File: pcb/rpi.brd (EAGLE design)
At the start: 88 x 85 mm, 27 parts, among them IC1 LD117AS33TR, SW1 324_SW, SW20 324_SW, U5 CH340C

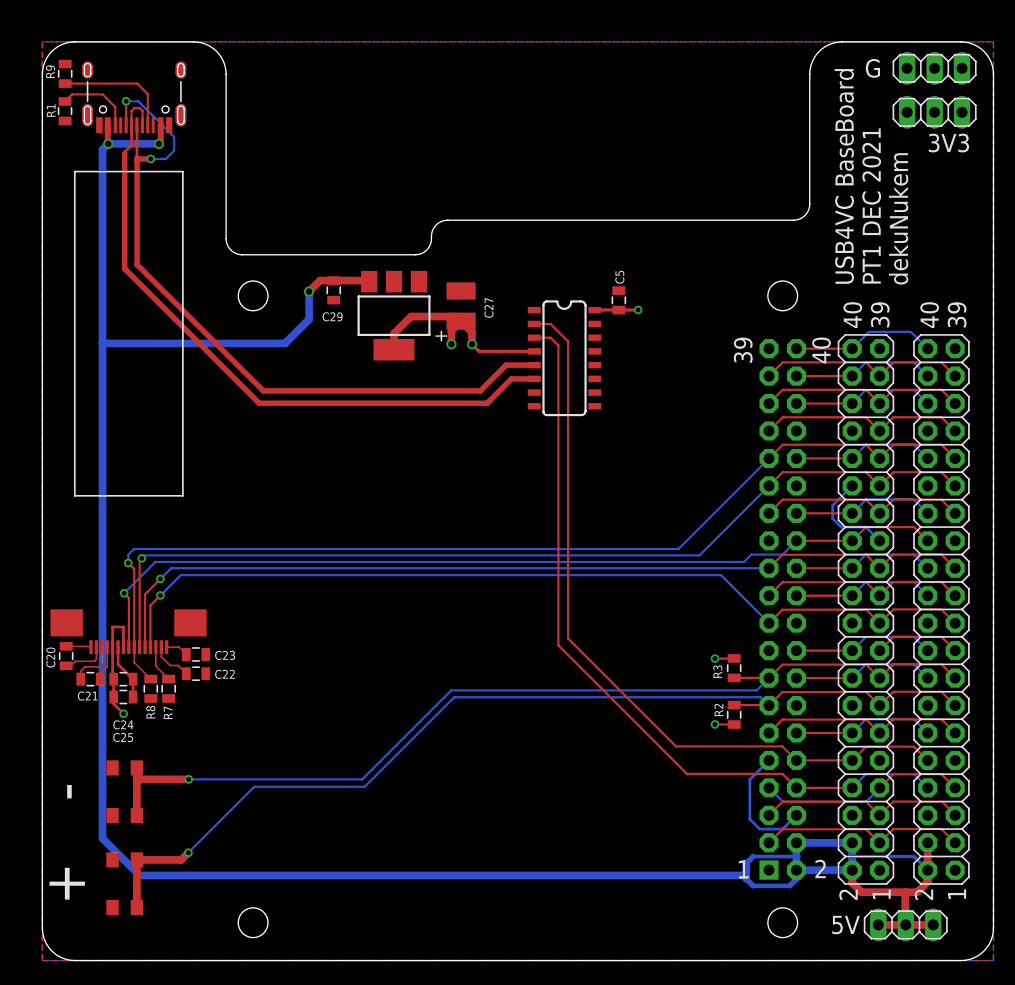
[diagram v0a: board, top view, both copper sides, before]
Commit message: updated baseboard, added power buttons
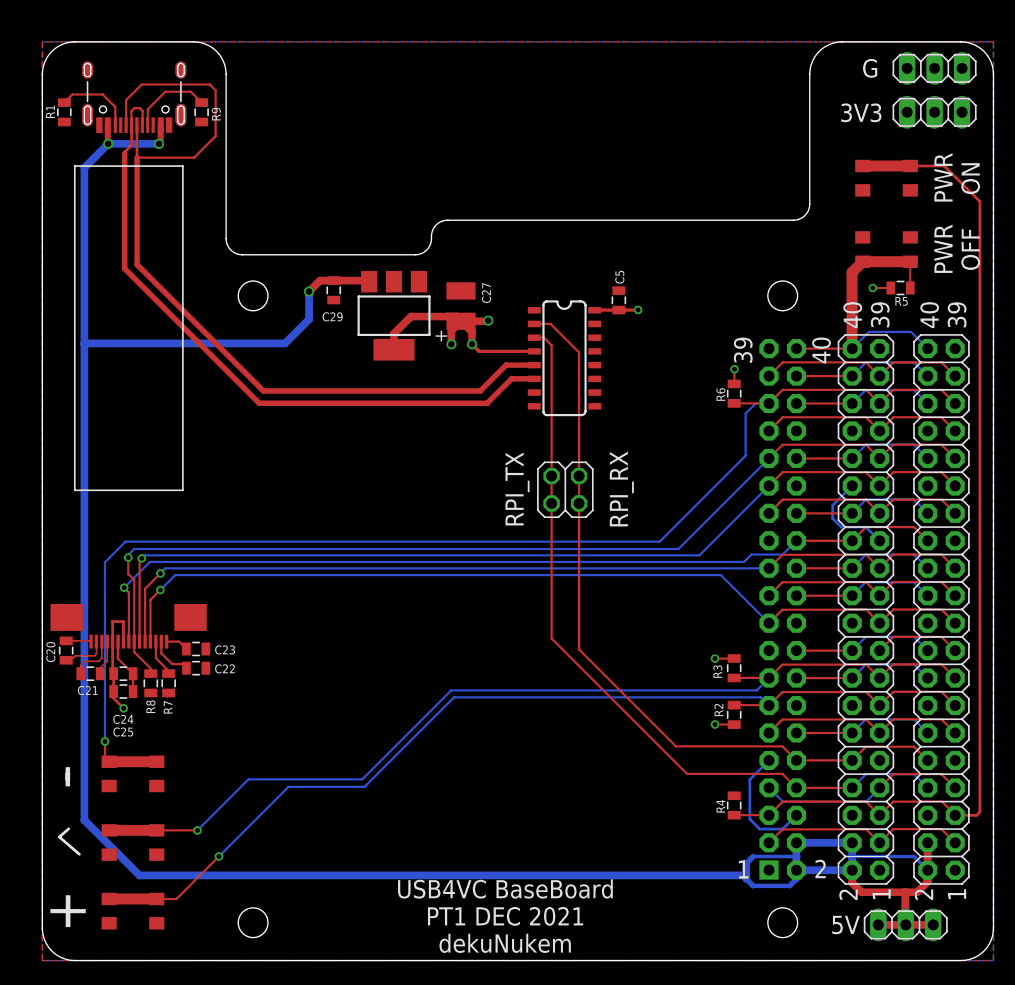
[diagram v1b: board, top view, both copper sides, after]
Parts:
- added JP7: (no value), pinhead:2X02
- added R4, R5, R6: 390K, SparkFun-Passives:0805
- added SW2, SW3, SW4: 324_SW, 3pos_slide_switch_centered:342_SWICH_FOOT
- moved R9 13.1 mm to (14.7, 78.5), turned to 270 degrees
- moved SW20 4.76 mm to (8.38, 10.9), turned to 0 degrees
- moved SW1 2.65 mm to (8.38, 4.57), turned to 0 degrees
- moved C20 0.51 mm to (2.20, 28.7)
- moved C21 0.51 mm to (4.45, 26.5)
- moved C22 0.51 mm to (14.2, 27.1)
- moved C23 0.51 mm to (14.2, 28.8)
- moved C24 0.51 mm to (7.49, 26.5)
- moved C25 0.51 mm to (7.49, 24.9)
- moved R7 0.51 mm to (11.7, 25.7)
- moved R8 0.51 mm to (10.0, 25.7)
- moved U2 0.51 mm to (8.00, 29.5)
- moved R1 0.13 mm to (2.03, 78.5)
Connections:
- net N$11 renamed ENTER_BUTTON
- net N$34 renamed PLUS_BUTTON
- removed net N$20: JP1.35, JP2.35, PCB1.P$35
- removed net UART0_RX: JP1.10, JP2.10, PCB1.P$10, U5.2
- removed net UART0_TX: JP1.8, JP2.8, PCB1.P$8, U5.3
- new net MINUS_BUTTON: JP1.35, JP2.35, PCB1.P$35, R6.1, SW4.P$2, SW4.P$3
- new net RPI_RX: JP1.10, JP2.10, JP7.1, JP7.2, PCB1.P$10, U5.2
- new net RPI_TX: JP1.8, JP2.8, JP7.3, JP7.4, PCB1.P$8, U5.3
- net +3V3: now also R5.2, R6.2
- net GND: now also SW2.P$1, SW2.P$4, SW3.P$1, SW3.P$4, SW4.P$1, SW4.P$4
- net N$32: now also R5.1, SW3.P$2, SW3.P$3
- net N$6: now also R4.1, SW2.P$2, SW2.P$3
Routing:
- net MINUS_BUTTON: track 0.00 -> 115.4 mm, vias 0 -> 1
- net N$6: track 19.4 -> 93.7 mm
- net UART0_TX: track 71.0 -> 0.00 mm
- net RPI_TX: track 0.00 -> 70.6 mm
- net UART0_RX: track 70.3 -> 0.00 mm
- net RPI_RX: track 0.00 -> 70.3 mm
- net N$20: track 19.3 -> 0.00 mm
- net N$32: track 13.4 -> 28.7 mm
- net N$1: track 68.6 -> 79.2 mm, vias 2 -> 0
- net +3V3: track 46.5 -> 52.1 mm, vias 6 -> 9
- net N$2: track 10.9 -> 7.53 mm
- net +5V: track 218.2 -> 221.3 mm
- net N$16: track 88.4 -> 87.9 mm
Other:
- board text added: "PWR OFF"
- board text added: "PWR ON"
- board text added: "RPI_RX"
- board text added: "RPI_TX"

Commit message: added i2c pullups, cleanup
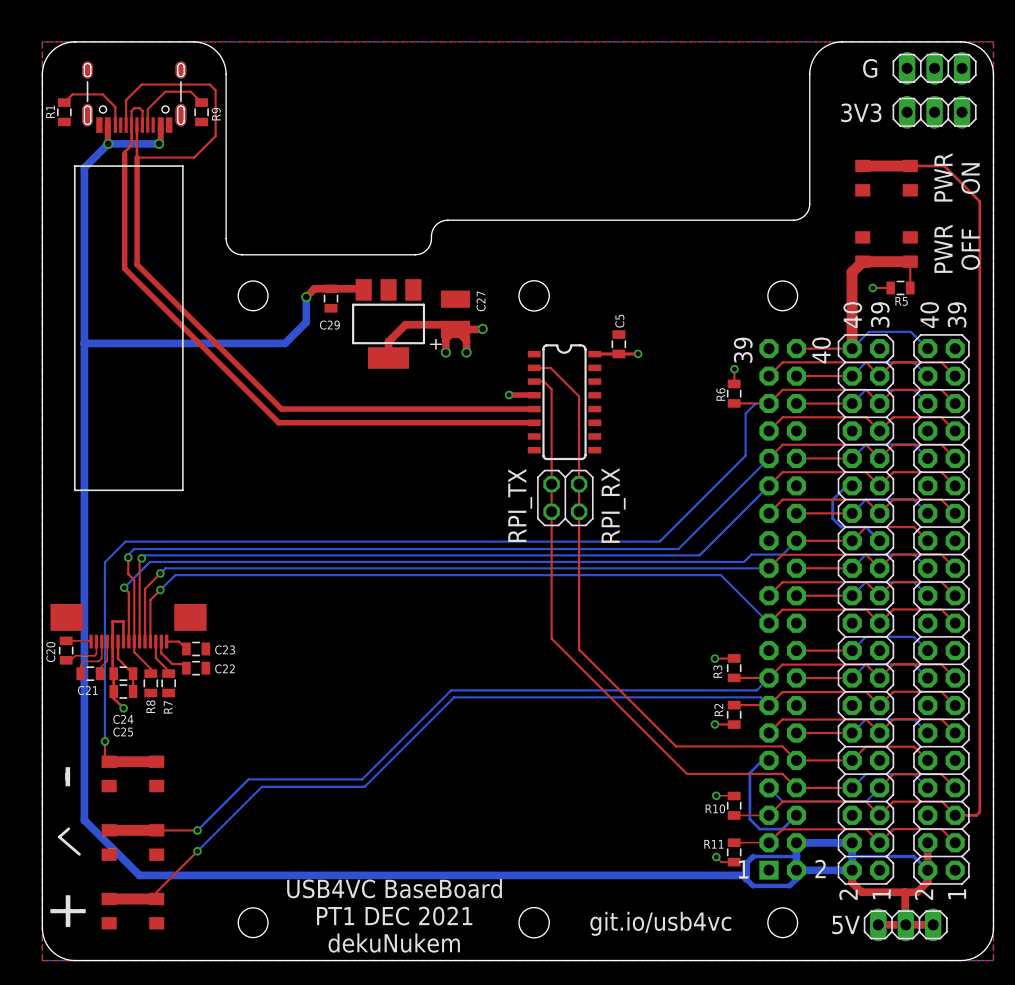
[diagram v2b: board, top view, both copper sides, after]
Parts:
- removed R4: 390K, SparkFun-Passives:0805
- added R10, R11: 5.1K, joyAnalog:0805
- added U$2, U$3: M2.5HOLE, f1c100s:M2.5HOLE
- moved C5 4.06 mm to (53.3, 57.0)
- moved U5 4.06 mm to (48.3, 51.7)
- moved C27 0.92 mm to (38.2, 59.8)
- moved IC1 0.92 mm to (32.0, 58.9)
- moved C29 0.80 mm to (26.7, 61.3)
- moved JP7 0.76 mm to (48.4, 42.8)
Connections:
- net +3V3: now also R10.1, R11.1
- net N$5: now also R11.2
- net N$6: now also R10.2; no longer R4.1
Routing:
- net +3V3: track 52.1 -> 43.9 mm, vias 9 -> 12
- net RPI_RX: track 70.3 -> 66.2 mm
- net RPI_TX: track 70.6 -> 66.5 mm
- net N$5: track 19.3 -> 22.5 mm
- net +5V: track 221.3 -> 220.3 mm
- net GND: track 25.6 -> 26.2 mm
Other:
- board text added: "git.io/usb4vc"

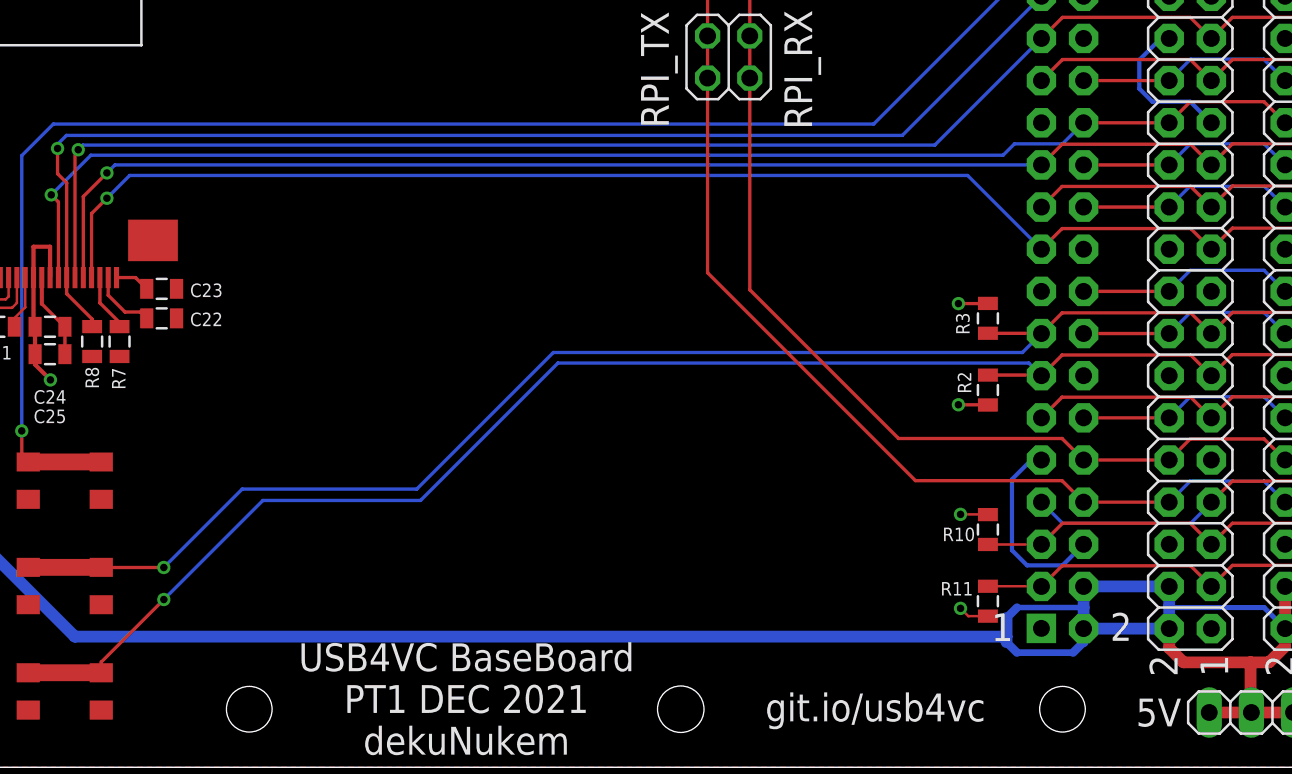
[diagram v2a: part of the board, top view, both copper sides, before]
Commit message: finished ADB protocol board
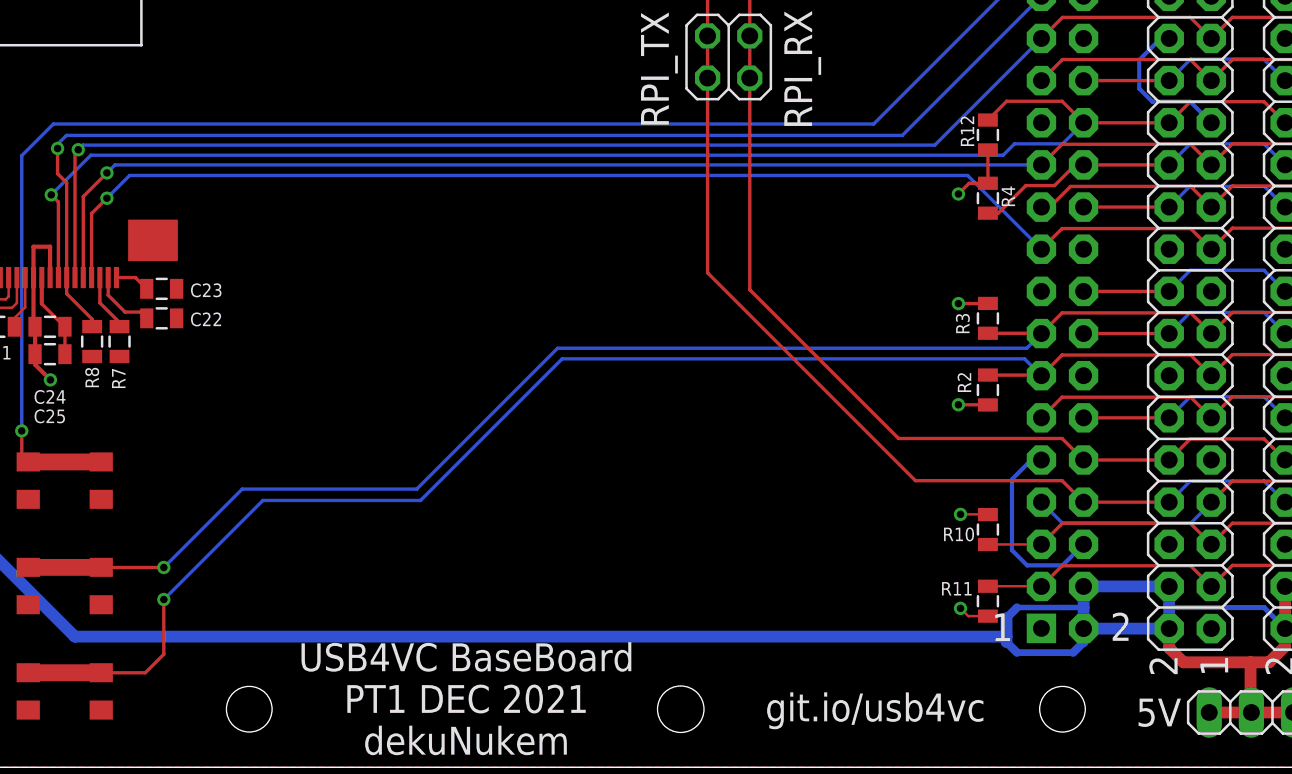
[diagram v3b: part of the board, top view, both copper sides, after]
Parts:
- added R12, R4: 5.1K, joyAnalog:0805
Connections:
- net +3V3: now also R12.1, R4.1
- net N$26: now also R4.2
- net N$27: now also R12.2
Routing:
- net N$26: track 13.2 -> 20.2 mm
- net N$27: track 82.4 -> 89.1 mm
- net +3V3: track 43.9 -> 47.9 mm, vias 12 -> 13
- net PLUS_BUTTON: track 92.0 -> 93.8 mm
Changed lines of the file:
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@@
 <element name="U$2" library="f1c100s" package="M2.5HOLE" value="M2.5HOLE" x="45.5" y="3.5" smashed="yes"/>
 <element name="U$3" library="f1c100s" package="M2.5HOLE" value="M2.5HOLE" x="45.5" y="61.5" smashed="yes"/>
+<element name="R4" library="joyAnalog" package="0805" value="5.1K" x="64.008" y="34.29" smashed="yes" rot="R270">
+<attribute name="NAME" x="64.8335" y="35.052" size="0.8128" layer="25" rot="R270"/>
+</element>
+<element name="R12" library="joyAnalog" package="0805" value="5.1K" x="64.008" y="38.1" smashed="yes" rot="R90">
+<attribute name="NAME" x="63.1825" y="37.338" size="0.8128" layer="25" rot="R90"/>
+</element>
 </elements>
 <signals>
@@
 <wire x1="43.18" y1="52.324" x2="45.4854" y2="52.324" width="0.508" layer="1"/>
 <wire x1="45.4854" y1="52.324" x2="45.5108" y2="52.2986" width="0.508" layer="1"/>
+<contactref element="R12" pad="1"/>
+<contactref element="R4" pad="1"/>
+<via x="62.23" y="34.544" extent="1-16" drill="0.45"/>
+<wire x1="64.008" y1="37.2" x2="64.008" y2="35.19" width="0.2032" layer="1"/>
+<wire x1="62.23" y1="34.544" x2="62.876" y2="35.19" width="0.2032" layer="1"/>
+<wire x1="62.876" y1="35.19" x2="64.008" y2="35.19" width="0.2032" layer="1"/>
 </signal>
 <signal name="+5V">
@@
 <wire x1="64.008" y1="26.151" x2="67.2174" y2="26.151" width="0.2032" layer="1"/>
 <wire x1="67.2174" y1="26.151" x2="67.2318" y2="26.1366" width="0.2032" layer="1"/>
-<wire x1="67.2318" y1="26.1366" x2="66.0888" y2="24.9936" width="0.2032" layer="16"/>
-<wire x1="66.0888" y1="24.9936" x2="37.8206" y2="24.9936" width="0.2032" layer="16"/>
+<wire x1="67.2318" y1="26.1366" x2="66.3428" y2="25.2476" width="0.2032" layer="16"/>
+<wire x1="66.3428" y1="25.2476" x2="38.0746" y2="25.2476" width="0.2032" layer="16"/>
 <via x="14.351" y="12.0396" extent="1-16" drill="0.45"/>
-<wire x1="37.8206" y1="24.9936" x2="29.591" y2="16.764" width="0.2032" layer="16"/>
+<wire x1="38.0746" y1="25.2476" x2="29.591" y2="16.764" width="0.2032" layer="16"/>
 <wire x1="29.591" y1="16.764" x2="19.0754" y2="16.764" width="0.2032" layer="16"/>
 <wire x1="19.0754" y1="16.764" x2="14.351" y2="12.0396" width="0.2032" layer="16"/>
@@
 <contactref element="JP1" pad="21"/>
 <contactref element="PCB1" pad="P$21"/>
-<wire x1="67.2318" y1="33.7566" x2="68.4764" y2="35.0012" width="0.2032" layer="1"/>
-<wire x1="68.4764" y1="35.0012" x2="76.2254" y2="35.0012" width="0.2032" layer="1"/>
+<wire x1="68.9844" y1="35.0012" x2="67.7398" y2="33.7566" width="0.2032" layer="1"/>
+<wire x1="67.2318" y1="33.7566" x2="67.7398" y2="33.7566" width="0.2032" layer="1"/>
+<wire x1="68.9844" y1="35.0012" x2="76.2254" y2="35.0012" width="0.2032" layer="1"/>
 <wire x1="76.2254" y1="35.0012" x2="77.47" y2="33.7566" width="0.2032" layer="1"/>
 <contactref element="JP2" pad="21"/>
@@
 <wire x1="80.645" y1="37.5666" x2="81.915" y2="36.2966" width="0.2032" layer="16"/>
 <wire x1="76.2" y1="37.5666" x2="80.645" y2="37.5666" width="0.2032" layer="16"/>
+<contactref element="R4" pad="2"/>
+<wire x1="69.7718" y1="36.2966" x2="69.2658" y2="36.2966" width="0.2032" layer="1"/>
+<wire x1="68.0212" y1="35.052" x2="66.294" y2="35.052" width="0.2032" layer="1"/>
+<wire x1="69.2658" y1="36.2966" x2="68.0212" y2="35.052" width="0.2032" layer="1"/>
+<wire x1="64.632" y1="33.39" x2="64.008" y2="33.39" width="0.2032" layer="1"/>
+<wire x1="66.294" y1="35.052" x2="64.632" y2="33.39" width="0.2032" layer="1"/>
 </signal>
 <signal name="N$27">
@@
 <wire x1="65.6082" y1="37.5666" x2="64.9224" y2="36.8808" width="0.2032" layer="16"/>
 <wire x1="64.9224" y1="36.8808" x2="9.9568" y2="36.8808" width="0.2032" layer="16"/>
+<contactref element="R12" pad="2"/>
+<wire x1="64.008" y1="39" x2="65.14" y2="40.132" width="0.2032" layer="1"/>
+<wire x1="68.4764" y1="40.132" x2="69.7718" y2="38.8366" width="0.2032" layer="1"/>
+<wire x1="65.14" y1="40.132" x2="68.4764" y2="40.132" width="0.2032" layer="1"/>
 </signal>
 <signal name="N$28">
@@
 <wire x1="64.008" y1="23.633" x2="67.1954" y2="23.633" width="0.2032" layer="1"/>
 <wire x1="67.1954" y1="23.633" x2="67.2318" y2="23.5966" width="0.2032" layer="1"/>
-<wire x1="67.2318" y1="23.5966" x2="66.4698" y2="24.3586" width="0.2032" layer="16"/>
-<wire x1="66.4698" y1="24.3586" x2="38.1" y2="24.3586" width="0.2032" layer="16"/>
+<wire x1="67.2318" y1="23.5966" x2="66.2158" y2="24.6126" width="0.2032" layer="16"/>
+<wire x1="66.2158" y1="24.6126" x2="38.354" y2="24.6126" width="0.2032" layer="16"/>
 <wire x1="20.32" y1="16.0782" x2="14.351" y2="10.1092" width="0.2032" layer="16"/>
 <via x="14.351" y="10.1092" extent="1-16" drill="0.45"/>
-<wire x1="38.1" y1="24.3586" x2="29.8196" y2="16.0782" width="0.2032" layer="16"/>
+<wire x1="38.354" y1="24.6126" x2="29.8196" y2="16.0782" width="0.2032" layer="16"/>
 <wire x1="29.8196" y1="16.0782" x2="20.32" y2="16.0782" width="0.2032" layer="16"/>
-<wire x1="14.351" y1="10.1092" x2="10.582" y2="6.3402" width="0.2032" layer="1"/>
-<wire x1="10.582" y1="5.697" x2="10.582" y2="6.3402" width="0.2032" layer="1"/>
+<wire x1="14.351" y1="10.1092" x2="14.351" y2="6.8072" width="0.2032" layer="1"/>
+<wire x1="14.351" y1="6.8072" x2="13.2408" y2="5.697" width="0.2032" layer="1"/>
+<wire x1="10.582" y1="5.697" x2="13.2408" y2="5.697" width="0.2032" layer="1"/>
 <wire x1="6.182" y1="5.697" x2="10.582" y2="5.697" width="1.016" layer="1"/>
 </signal>
